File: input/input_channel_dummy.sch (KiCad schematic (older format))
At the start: 0 parts

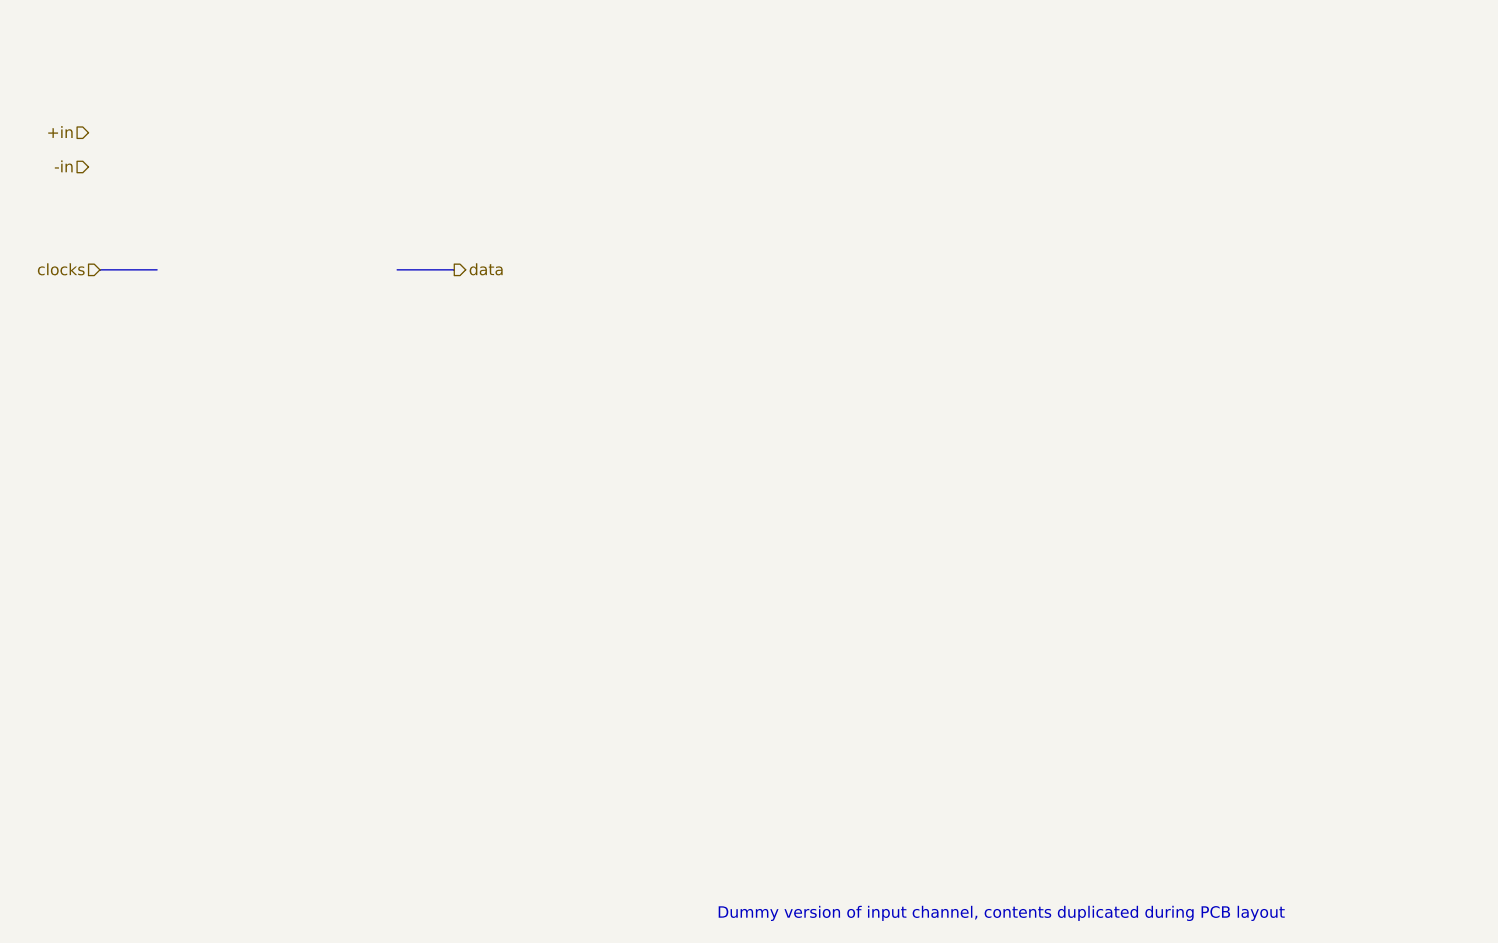
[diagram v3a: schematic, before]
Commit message: Cleanup to get ready to start board layout. I had to get rid off all the bus signals, since in Kicad busses don't work that way.  Added a couple testpoints; many more needed.
Work on component placement in PCB.  I changed DGND to plain GND and "protective earth" to
"earth" (for chassis ground).  Chassis ground is now connected on the board only via a capacitor.
I had to fix the connector footprint to match the pin numbers on the symbol (there was a case
difference).
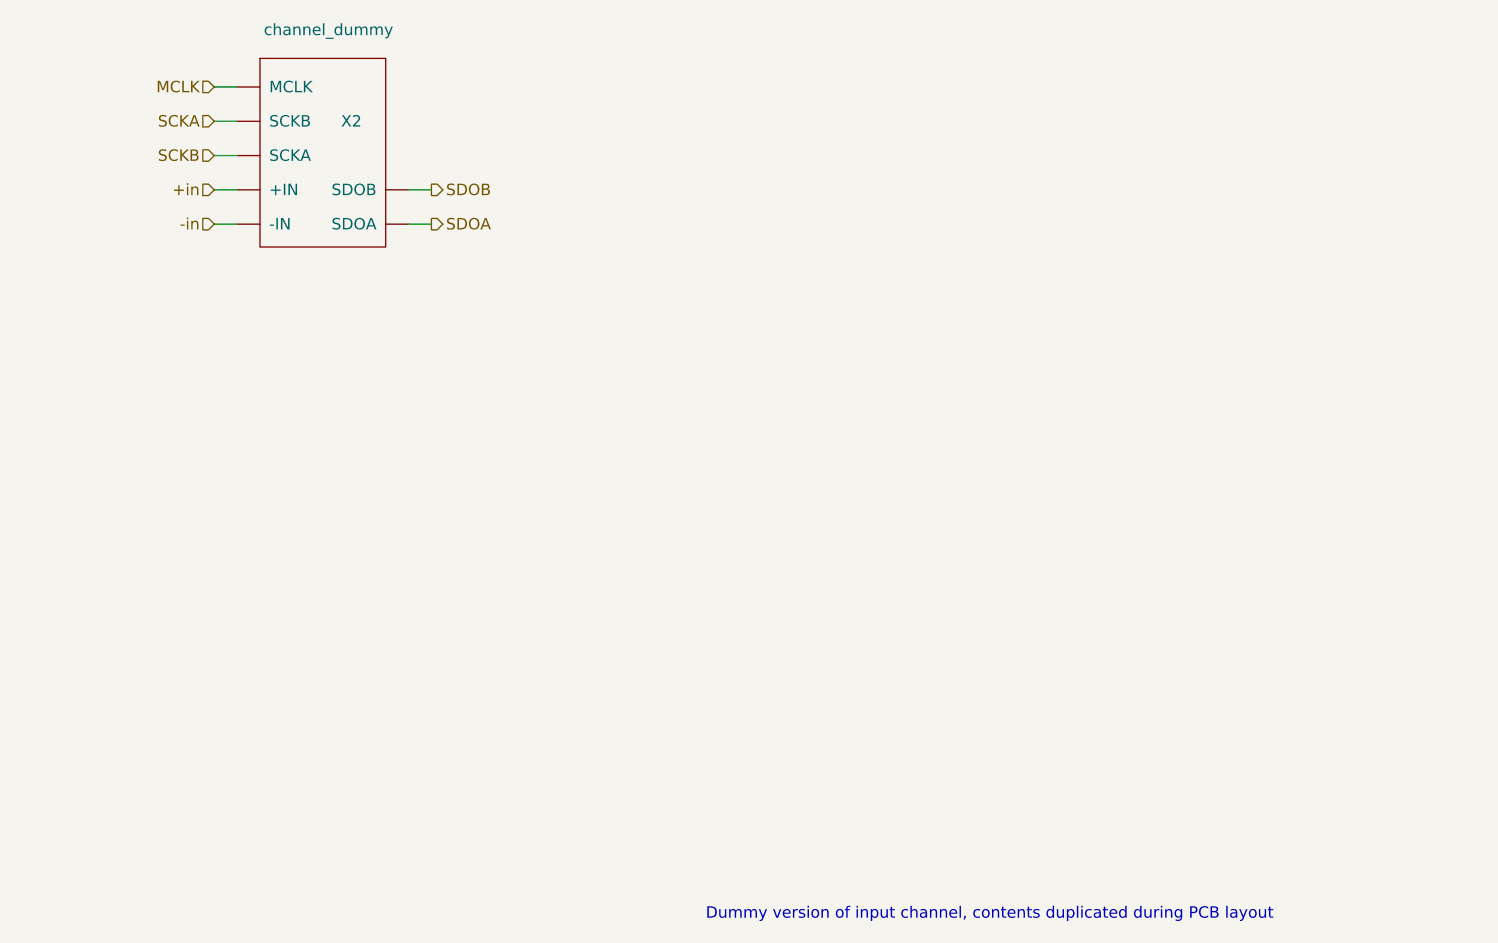
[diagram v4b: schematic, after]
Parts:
- added X1: channel_dummy, input:channel_dummy, symbol ilemt_input:channel_dummy
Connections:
- net +in: now also X1.4 (+IN)
- net -in: now also X1.5 (-IN)
- new net MCLK: X1.1 (MCLK)
- new net SCKA: X1.2 (SCKB)
- new net SCKB: X1.3 (SCKA)
- new net SDOA: X1.6 (SDOA)
- new net SDOB: X1.7 (SDOB)
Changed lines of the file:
@@
 Comment4 ""
 $EndDescr
-Text Notes 7150 6750 0    50   ~ 0
+Text Notes 7100 6750 0    50   ~ 0
 Dummy version of input channel, contents duplicated during PCB layout
-Text HLabel 6000 3900 2    50   Output ~ 0
-data
-Text HLabel 4400 3300 0    50   Input ~ 0
+Wire Wire Line
+	4950 3700 5050 3700
+Wire Wire Line
+	4950 3550 5050 3550
+$Comp
+L ilemt_input:channel_dummy X1
+U 1 1 5E89BCC9
+P 5450 3400
+AR Path="/5E194E0B/5E89BCC9" Ref="X1"  Part="1"
+AR Path="/5E1F318C/5E89BCC9" Ref="X2"  Part="1"
+F 0 "X2" V 5300 3300 50  0000 C CNN
+F 1 "channel_dummy" V 4900 3400 50  0000 C CNN
+F 2 "input:channel_dummy" H 5450 3400 50  0001 C CNN
+F 3 "" H 5450 3400 50  0001 C CNN
+	1    5450 3400
+	0    -1   1    0
+$EndComp
+Text HLabel 4950 3700 0    50   Input ~ 0
+-in
+Text HLabel 4950 3550 0    50   Input ~ 0
 +in
-Text HLabel 4400 3450 0    50   Input ~ 0
--in
-Text HLabel 4450 3900 0    50   Input ~ 0
-clocks
-Wire Bus Line
-	4700 3900 4450 3900
-Wire Bus Line
-	5750 3900 6000 3900
+Text HLabel 5900 3700 2    50   Output ~ 0
+SDOA
+Text HLabel 5900 3550 2    50   Output ~ 0
+SDOB
+Text HLabel 4950 3100 0    50   Input ~ 0
+MCLK
+Text HLabel 4950 3400 0    50   Input ~ 0
+SCKB
+Text HLabel 4950 3250 0    50   Input ~ 0
+SCKA
+Wire Wire Line
+	4950 3100 5050 3100
+Wire Wire Line
+	4950 3250 5050 3250
+Wire Wire Line
+	4950 3400 5050 3400
+Wire Wire Line
+	5900 3550 5800 3550
+Wire Wire Line
+	5900 3700 5800 3700
 $EndSCHEMATC

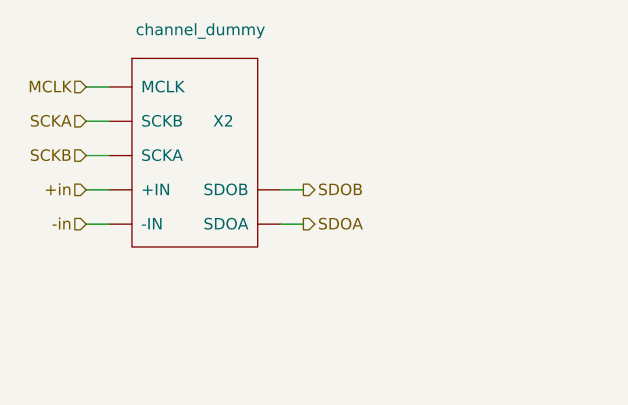
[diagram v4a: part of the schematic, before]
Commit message: Progress on input board layout.  Have adopted 100x280mm eurocard format with connector at the back. Schematic changes are mostly cosmetic.  The working board file is now input/input_board_rear.kicad_pcb
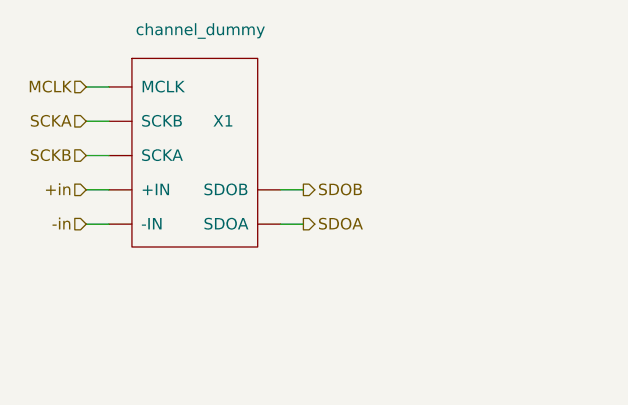
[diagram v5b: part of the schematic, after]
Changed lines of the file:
@@
 AR Path="/5E194E0B/5E89BCC9" Ref="X1"  Part="1"
 AR Path="/5E1F318C/5E89BCC9" Ref="X2"  Part="1"
-F 0 "X2" V 5300 3300 50  0000 C CNN
+F 0 "X1" V 5300 3300 50  0000 C CNN
 F 1 "channel_dummy" V 4900 3400 50  0000 C CNN
 F 2 "input:channel_dummy" H 5450 3400 50  0001 C CNN

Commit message: Changed board connector to PCIe 8x, added test points, cleanup of component values. Add LVDS Rx termination, bypass caps.
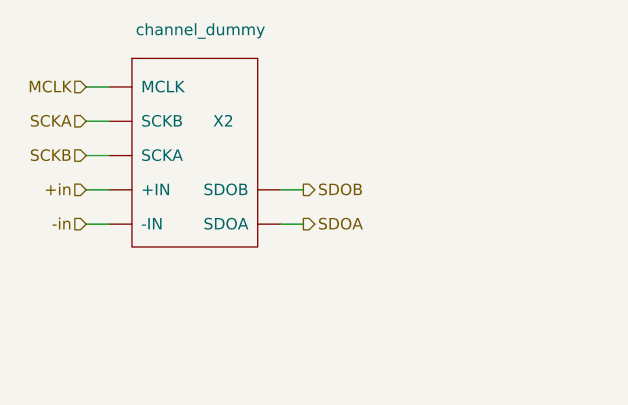
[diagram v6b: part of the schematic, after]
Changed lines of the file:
@@
 AR Path="/5E194E0B/5E89BCC9" Ref="X1"  Part="1"
 AR Path="/5E1F318C/5E89BCC9" Ref="X2"  Part="1"
-F 0 "X1" V 5300 3300 50  0000 C CNN
+F 0 "X2" V 5300 3300 50  0000 C CNN
 F 1 "channel_dummy" V 4900 3400 50  0000 C CNN
 F 2 "input:channel_dummy" H 5450 3400 50  0001 C CNN

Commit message: Snapshot before replicating input channels
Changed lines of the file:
@@
 AR Path="/5E194E0B/5E89BCC9" Ref="X1"  Part="1"
 AR Path="/5E1F318C/5E89BCC9" Ref="X2"  Part="1"
-F 0 "X2" V 5300 3300 50  0000 C CNN
+F 0 "X?" V 5300 3300 50  0000 C CNN
 F 1 "channel_dummy" V 4900 3400 50  0000 C CNN
 F 2 "input:channel_dummy" H 5450 3400 50  0001 C CNN
